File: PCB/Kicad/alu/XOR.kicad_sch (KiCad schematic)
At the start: 4 parts, among them U14 74LS86, U15 74LS86, U5 74LS86, U6 74LS86

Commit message: UPDATE
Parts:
- added C10, C11, C12, C13: 10n, symbol Device:C
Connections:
- net GND: now also C10.2, C11.2, C12.2, C13.2
- net VCC: now also C10.1, C11.1, C12.1, C13.1
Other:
- moved on the sheet: U14E, U15E, U5E

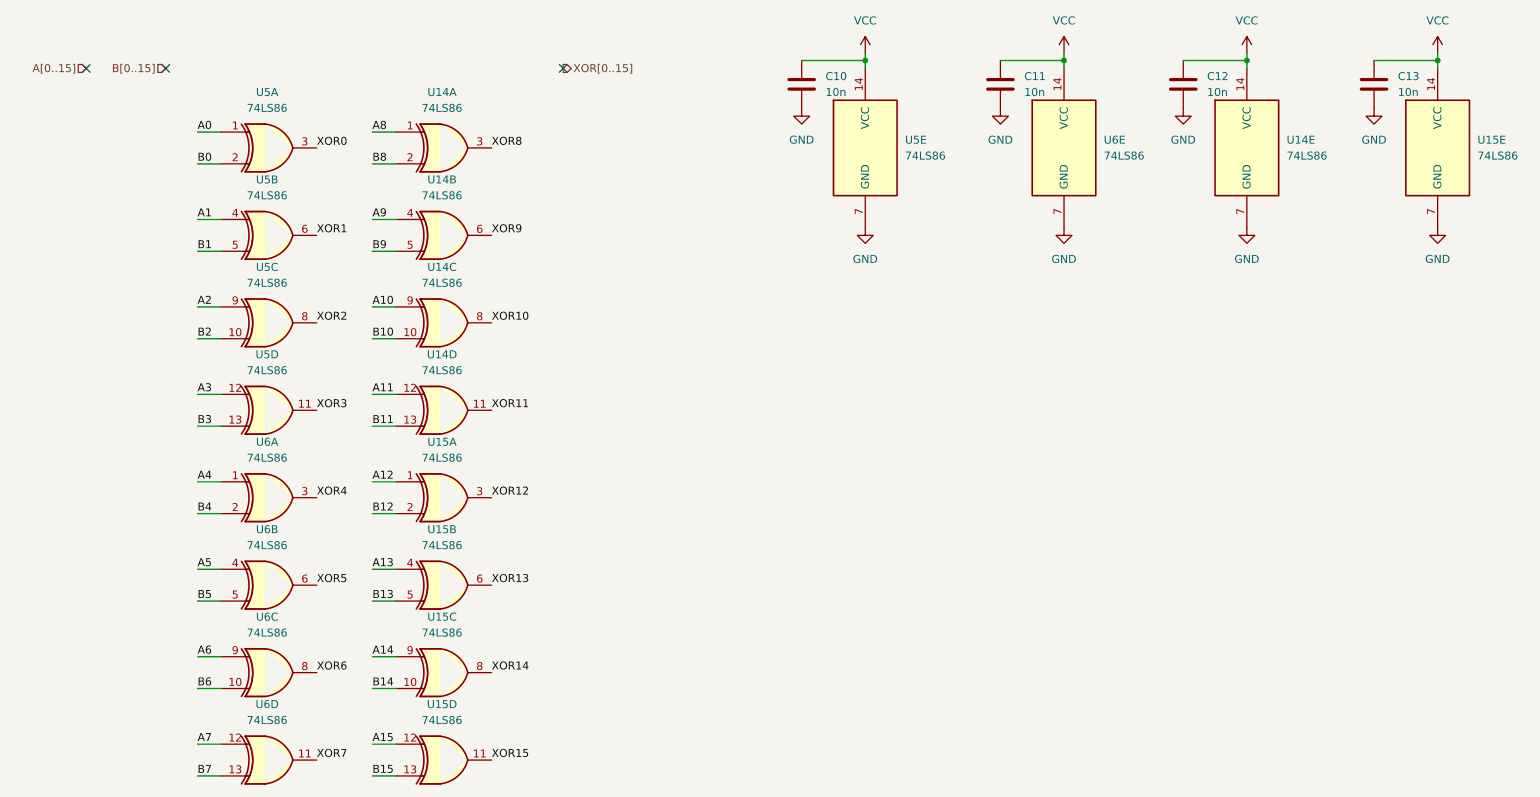
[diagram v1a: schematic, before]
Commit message: LEDs added
REGISTER.kicad_sch LEDs added to both REG_A and REG_B
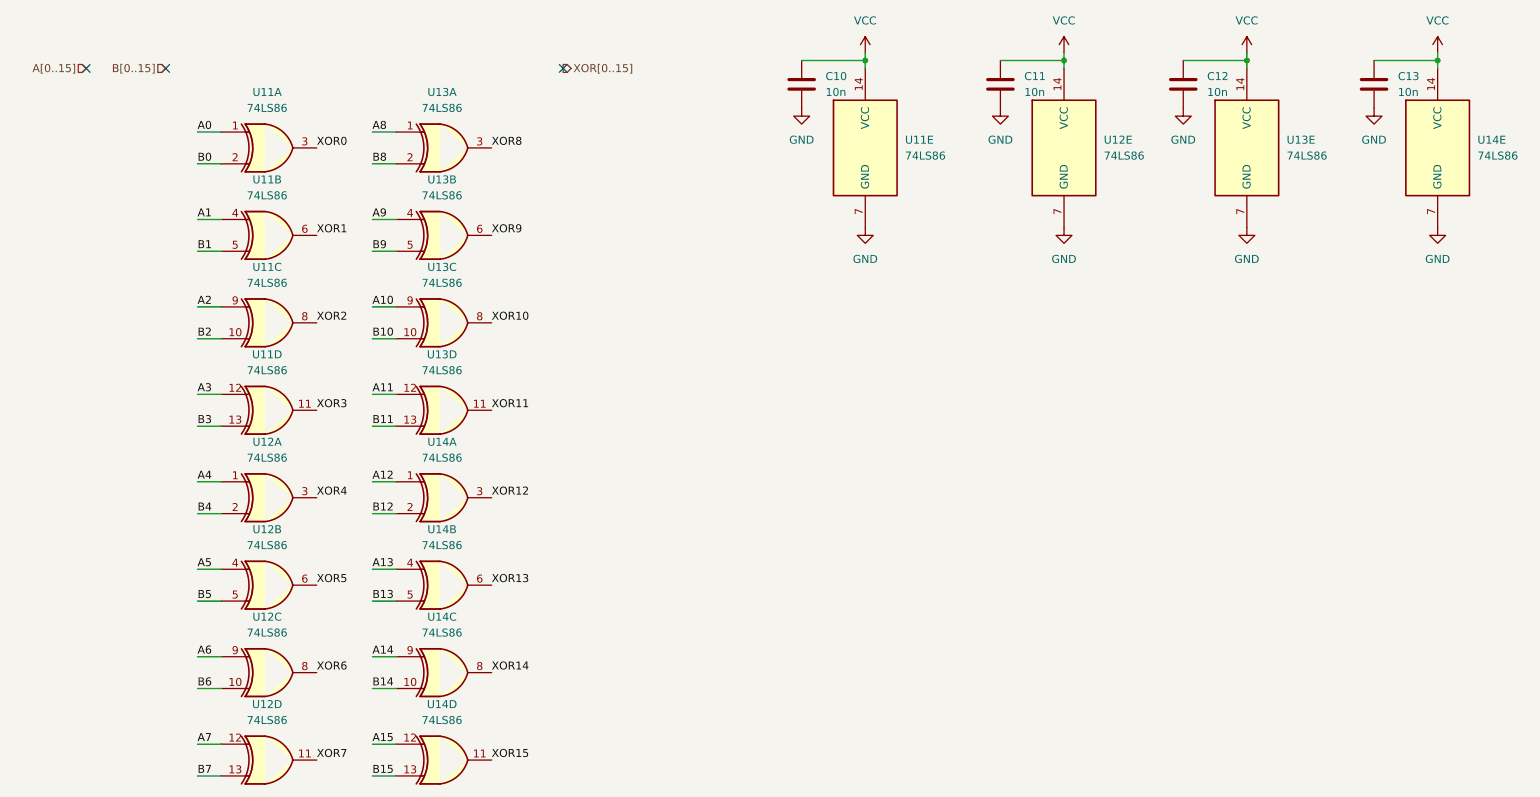
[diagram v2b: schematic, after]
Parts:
- renumbered U5 to U11, U6 to U12, U14 to U13, U15 to U14

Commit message: Footprints, PCB update
Added footprints to all components, updated the PCB with the schematic
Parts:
- C10, C11, C12, C13: footprint (none) -> Capacitor_SMD:C_0603_1608Metric
- U11, U12, U13, U14: footprint (none) -> Package_SO:SOIC-14_3.9x8.7mm_P1.27mm
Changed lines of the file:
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@@
 			)
 		)
-		(property "Footprint" ""
+		(property "Footprint" "Capacitor_SMD:C_0603_1608Metric"
 			(at 172.4152 39.37 0)
 			(effects
@@
 			)
 		)
-		(property "Footprint" ""
+		(property "Footprint" "Capacitor_SMD:C_0603_1608Metric"
 			(at 140.6652 39.37 0)
 			(effects
@@
 			)
 		)
-		(property "Footprint" ""
+		(property "Footprint" "Package_SO:SOIC-14_3.9x8.7mm_P1.27mm"
 			(at 241.3 45.72 0)
 			(effects
@@
 			)
 		)
-		(property "Footprint" ""
+		(property "Footprint" "Package_SO:SOIC-14_3.9x8.7mm_P1.27mm"
 			(at 54.61 73.66 0)
 			(effects
@@
 			)
 		)
-		(property "Footprint" ""
+		(property "Footprint" "Package_SO:SOIC-14_3.9x8.7mm_P1.27mm"
 			(at 82.55 129.54 0)
 			(effects
@@
 			)
 		)
-		(property "Footprint" ""
+		(property "Footprint" "Package_SO:SOIC-14_3.9x8.7mm_P1.27mm"
 			(at 54.61 101.6 0)
 			(effects
@@
 			)
 		)
-		(property "Footprint" ""
+		(property "Footprint" "Package_SO:SOIC-14_3.9x8.7mm_P1.27mm"
 			(at 82.55 87.63 0)
 			(effects
@@
 			)
 		)
-		(property "Footprint" ""
+		(property "Footprint" "Package_SO:SOIC-14_3.9x8.7mm_P1.27mm"
 			(at 82.55 115.57 0)
 			(effects
@@
 			)
 		)
-		(property "Footprint" ""
+		(property "Footprint" "Package_SO:SOIC-14_3.9x8.7mm_P1.27mm"
 			(at 54.61 143.51 0)
 			(effects
@@
 			)
 		)
-		(property "Footprint" ""
+		(property "Footprint" "Package_SO:SOIC-14_3.9x8.7mm_P1.27mm"
 			(at 82.55 45.72 0)
 			(effects
@@
 			)
 		)
-		(property "Footprint" ""
+		(property "Footprint" "Package_SO:SOIC-14_3.9x8.7mm_P1.27mm"
 			(at 54.61 45.72 0)
 			(effects
@@
 			)
 		)
-		(property "Footprint" ""
+		(property "Footprint" "Package_SO:SOIC-14_3.9x8.7mm_P1.27mm"
 			(at 54.61 129.54 0)
 			(effects
@@
 			)
 		)
-		(property "Footprint" ""
+		(property "Footprint" "Capacitor_SMD:C_0603_1608Metric"
 			(at 232.1052 39.37 0)
 			(effects
@@
 			)
 		)
-		(property "Footprint" ""
+		(property "Footprint" "Package_SO:SOIC-14_3.9x8.7mm_P1.27mm"
 			(at 181.61 45.72 0)
 			(effects
@@
 			)
 		)
-		(property "Footprint" ""
+		(property "Footprint" "Package_SO:SOIC-14_3.9x8.7mm_P1.27mm"
 			(at 210.82 45.72 0)
 			(effects
@@
 			)
 		)
-		(property "Footprint" ""
+		(property "Footprint" "Package_SO:SOIC-14_3.9x8.7mm_P1.27mm"
 			(at 54.61 115.57 0)
 			(effects
@@
 			)
 		)
-		(property "Footprint" ""
+		(property "Footprint" "Package_SO:SOIC-14_3.9x8.7mm_P1.27mm"
 			(at 82.55 59.69 0)
 			(effects
@@
 			)
 		)
-		(property "Footprint" ""
+		(property "Footprint" "Package_SO:SOIC-14_3.9x8.7mm_P1.27mm"
 			(at 54.61 59.69 0)
 			(effects
@@
 			)
 		)
-		(property "Footprint" ""
+		(property "Footprint" "Package_SO:SOIC-14_3.9x8.7mm_P1.27mm"
 			(at 149.86 45.72 0)
 			(effects
@@
 			)
 		)
-		(property "Footprint" ""
+		(property "Footprint" "Package_SO:SOIC-14_3.9x8.7mm_P1.27mm"
 			(at 54.61 87.63 0)
 			(effects
@@
 			)
 		)
-		(property "Footprint" ""
+		(property "Footprint" "Package_SO:SOIC-14_3.9x8.7mm_P1.27mm"
 			(at 82.55 143.51 0)
 			(effects
@@
 			)
 		)
-		(property "Footprint" ""
+		(property "Footprint" "Package_SO:SOIC-14_3.9x8.7mm_P1.27mm"
 			(at 82.55 73.66 0)
 			(effects
@@
 			)
 		)
-		(property "Footprint" ""
+		(property "Footprint" "Package_SO:SOIC-14_3.9x8.7mm_P1.27mm"
 			(at 82.55 101.6 0)
 			(effects
@@
 			)
 		)
-		(property "Footprint" ""
+		(property "Footprint" "Capacitor_SMD:C_0603_1608Metric"
 			(at 201.6252 39.37 0)
 			(effects

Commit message: ALU Pcb update
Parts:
- C10, C11, C12, C13: value 10n -> 100nF; footprint Capacitor_SMD:C_0603_1608Metric -> Capacitor_SMD:C_0402_1005Metric
- U11, U12, U13, U14: value 74LS86 -> 7486; footprint Package_SO:SOIC-14_3.9x8.7mm_P1.27mm -> Package_SO:SO-14_3.9x8.65mm_P1.27mm
